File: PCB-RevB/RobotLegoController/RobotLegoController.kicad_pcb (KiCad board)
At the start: 4 copper layers, 80 x 105 mm, 733 parts, among them J1 DF11-10DP-2DSA, J10 RJ12, J11 RJ12, J12 RJ12, J13 RJ12, J14 RJ12, J2 Raspberry_Pi_2_3, J3 USB_C_Receptacle_USB2.0, J4 Conn_01x02, J7 RJ12, J8 RJ12, J9 RJ12, Q1 BSS84, Q10 BSS84, Q11 BSS84, Q12 BSS84, Q13 2N7002, Q14 Si2371EDS, Q15 2N7002, Q16 2N7002, Q17 BSS84, Q18 BSS84, Q19 2N7002, Q2 BSS84, Q20 2N7002, Q21 Si2371EDS, Q27 2N7002, Q28 2N7002, Q29 2N7002, Q3 BSS84, Q30 2N7002, Q31 2N7002, Q32 2N7002, Q33 2N7002, Q34 2N7002, Q35 2N7002, Q36 2N7002, Q37 2N7002, Q4 2N7002, Q5 BSS84, Q6 BSS84, Q7 2N7002, Q8 2N7002, Q9 BSS84, SW1 SW_Omron_B3FS, SW2 SW_Omron_B3FS, SW3 SW_Omron_B3FS, SW5 SW_Omron_B3FS, U1 LSM6DSL, U10 LMV324, U11 LMV324, U12 LMV324, U13 SN74LVC1G14DBV, U14 SN74LVC1G14DBV, U15 SN74LVC1G14DBV, U16 SN74LVC1G14DBV, U17 DRV8833PWP, U18 LMV324, U19 SN74LVC1G14DBV, U2 STM32L496ZGTx, U20 SN74LVC1G14DBV, U21 SN74LVC1G14DBV, U22 SN74LVC1G14DBV, U23 DRV8833PWP, U3 SSD1306, U4 W25X40CLSS, U5 FUSB302B01MPX, U6 BQ25601, U7 AP2127K-3.3, U8 PAM2423AECADJR, U9 PAM2423AECADJR, Y2 8Z-24.000MAAJ-T

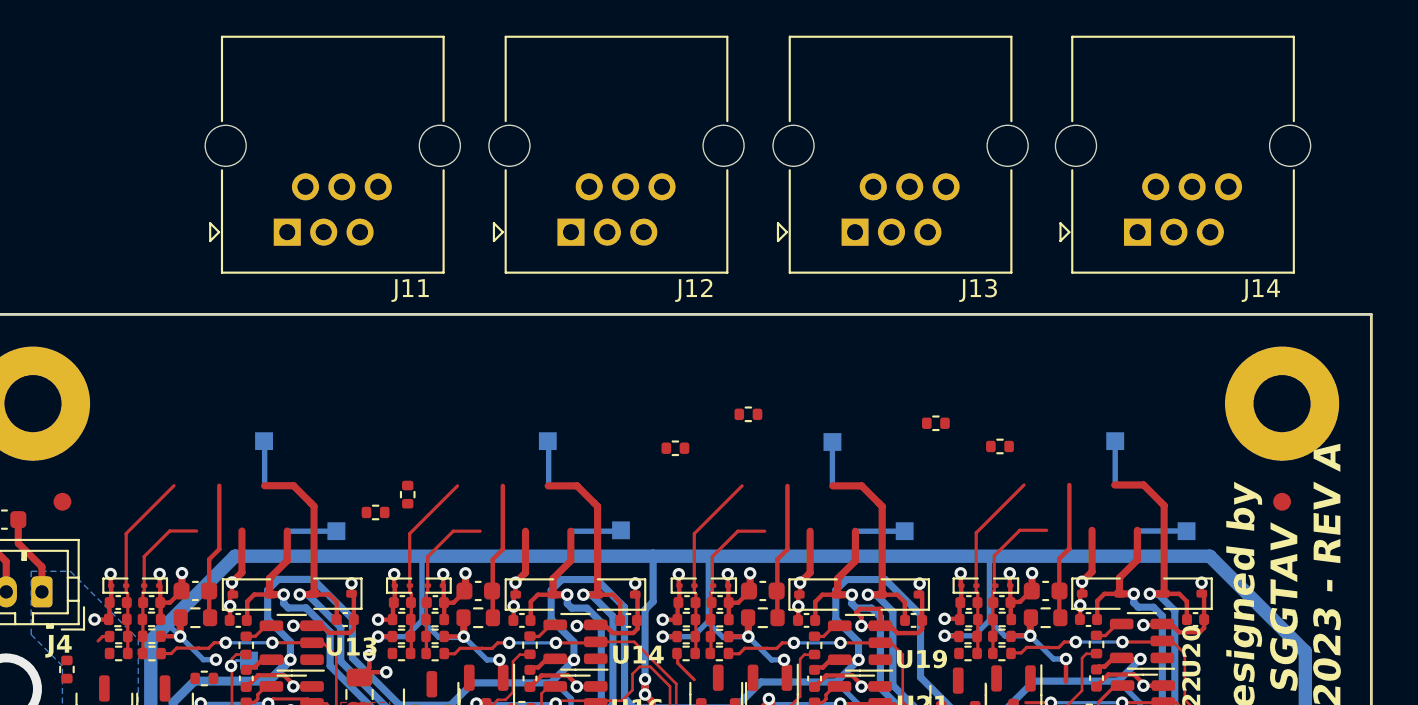
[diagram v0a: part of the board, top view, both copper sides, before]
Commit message: Alignment of the top connectors
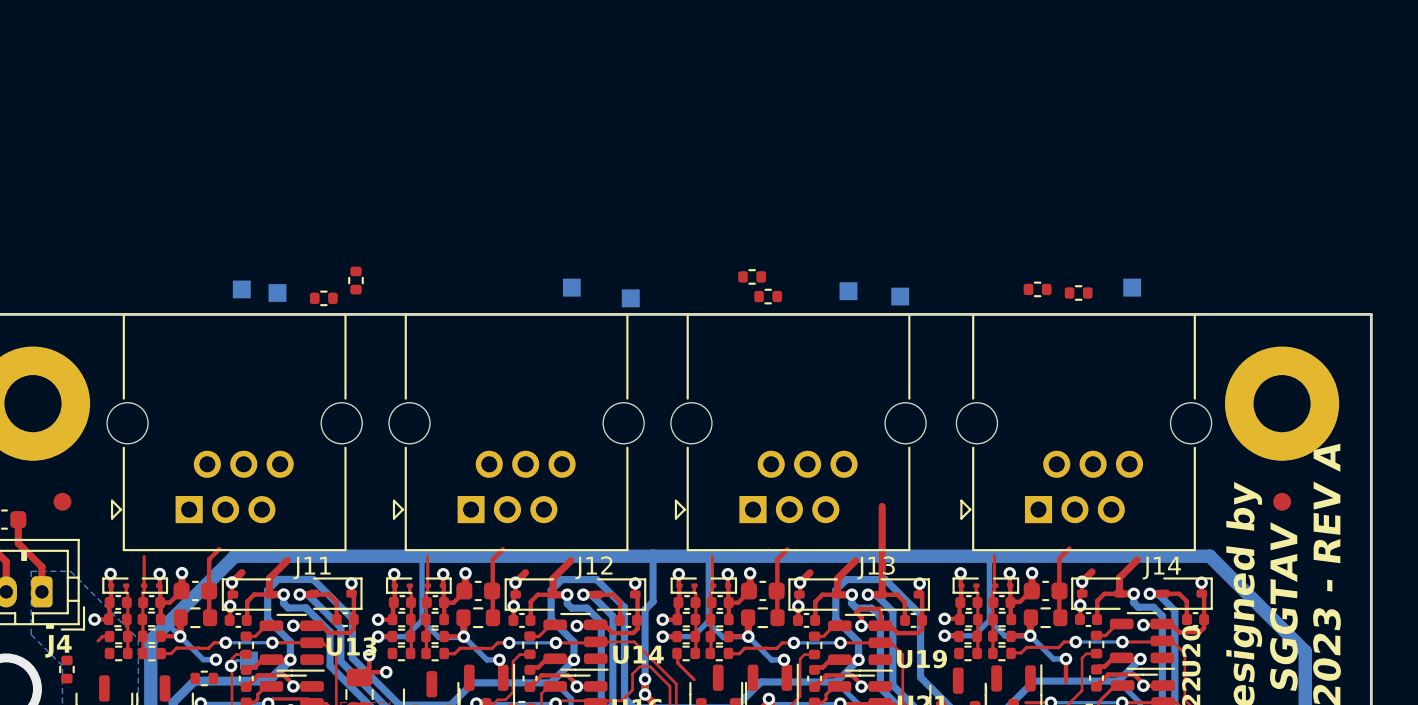
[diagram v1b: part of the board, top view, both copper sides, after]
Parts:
- removed TP130: S1mm, TestPoint:TestPoint_Pad_1.0x1.0mm
- moved J13 16.6 mm to (175.3, 44.9)
- moved J12 16.5 mm to (159.6, 44.9)
- moved J14 16.5 mm to (191.3, 44.9)
- moved J11 16.5 mm to (143.8, 44.9)
- moved TP110 13.8 mm to (148.7, 32.8)
- moved TP129 13.2 mm to (183.6, 33.0)
- moved TP111 13.0 mm to (168.5, 33.1)
- moved R248 12.3 mm to (153.1, 32.1)
- moved R249 12.3 mm to (151.3, 33.1)
- moved R155 10.5 mm to (175.3, 31.9)
- moved R251 9.66 mm to (193.6, 32.8)
- moved R250 9.42 mm to (191.3, 32.6)
- moved TP112 8.71 mm to (165.2, 32.5)
- moved TP131 8.65 mm to (196.6, 32.5)
- moved TP109 8.59 mm to (146.7, 32.6)
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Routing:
- net /05-System Outputs A/MOTORA_PIN2: track 34.8 -> 24.1 mm
- net /05-System Outputs A/MOTORB_PIN2: track 28.5 -> 17.9 mm
- net /06-System Outputs B/MOTORD_PIN2: track 36.8 -> 26.2 mm
- net GND: track 587.2 -> 577.9 mm
- net /06-System Outputs B/MOTORC_PIN6: track 10.5 -> 3.84 mm
- net /05-System Outputs A/MOTORA_PIN6: track 10.5 -> 3.84 mm
- net /05-System Outputs A/MOTORB_PIN6: track 10.5 -> 3.84 mm
- net /06-System Outputs B/MOTORD_PIN6: track 10.5 -> 3.84 mm
- net /06-System Outputs B/MOTORC_PIN2: track 28.9 -> 23.2 mm
- net /06-System Outputs B/MOTORD_PIN1: track 33.1 -> 28.7 mm
- net /06-System Outputs B/MOTORC_PIN1: track 25.1 -> 20.7 mm
- net /05-System Outputs A/MOTORA_PIN1: track 31.0 -> 26.6 mm
- net /05-System Outputs A/MOTORB_PIN1: track 25.2 -> 20.8 mm
- net Net-(C157-Pad2): track 7.65 -> 4.09 mm
- net Net-(C135-Pad2): track 7.65 -> 4.09 mm
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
